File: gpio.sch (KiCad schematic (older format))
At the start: 1 part, among them U1 LFE5U-85F-6BG381C

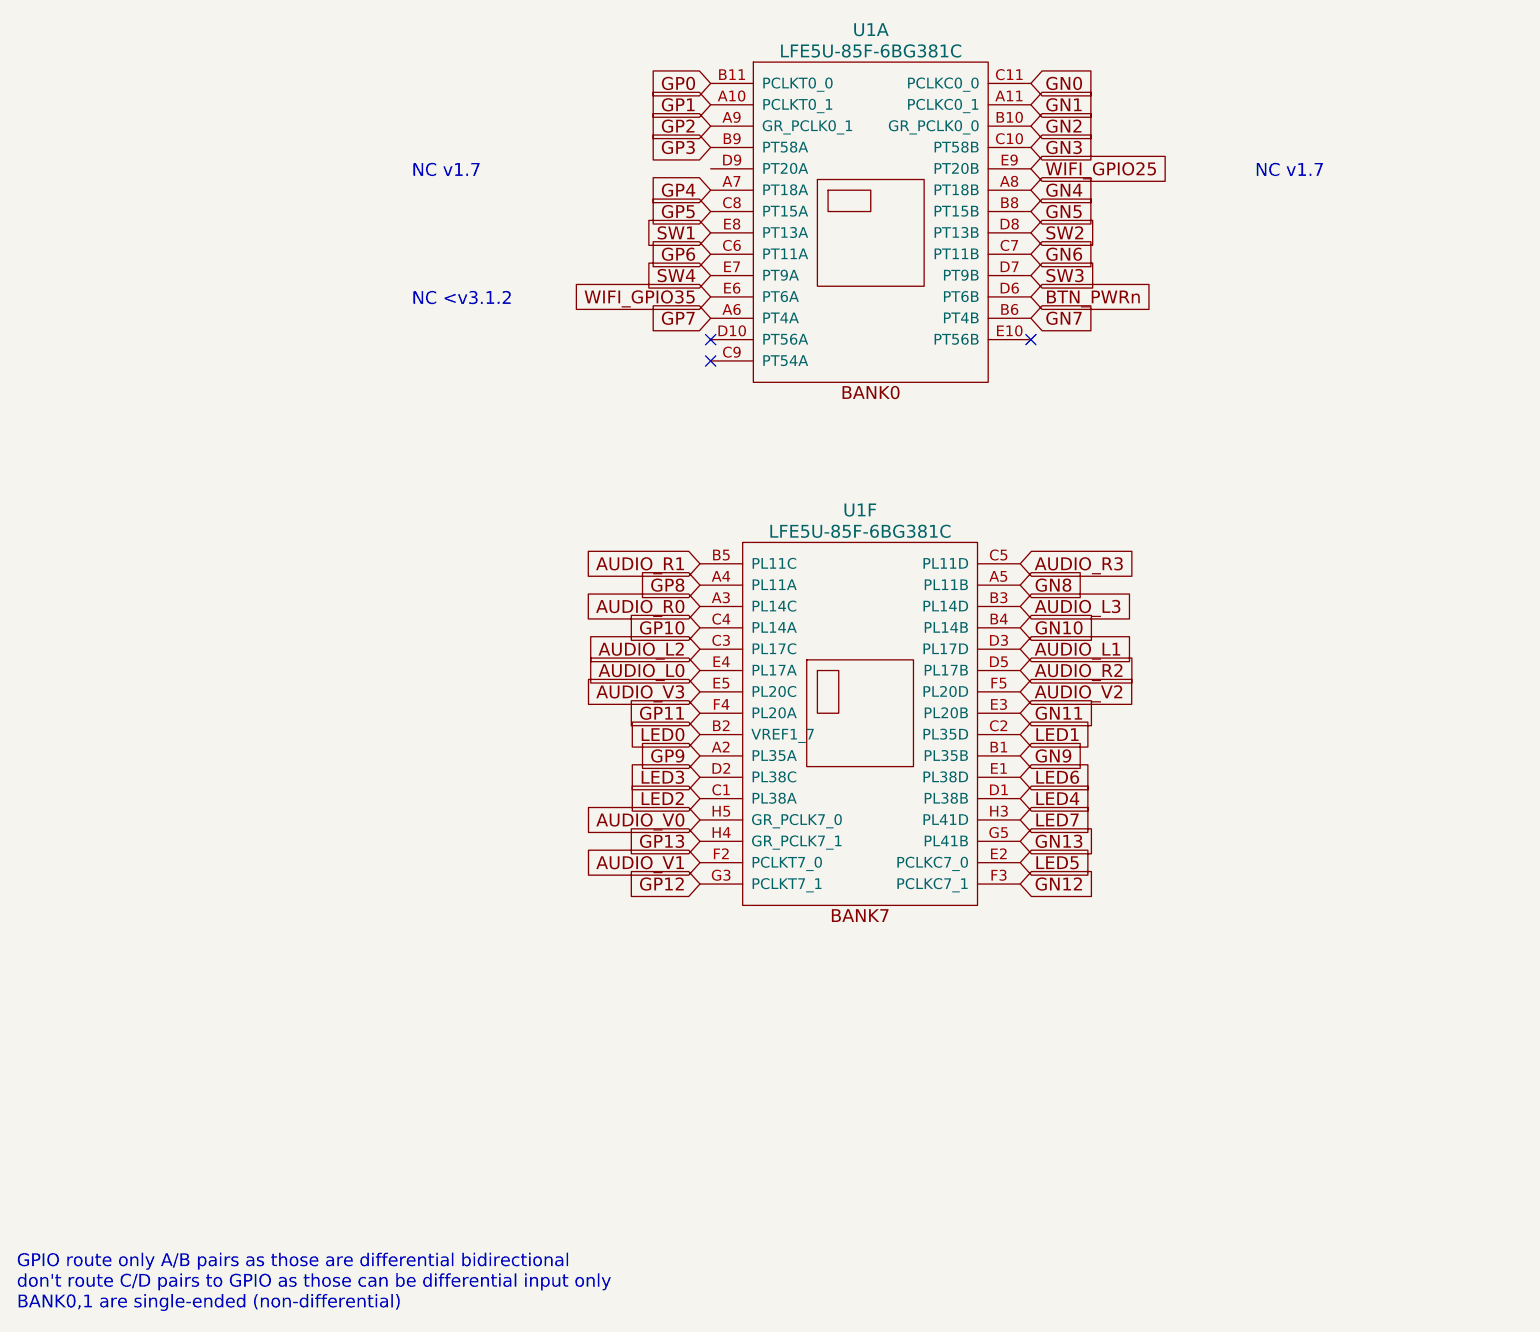
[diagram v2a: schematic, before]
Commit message: Rewiering LCD OUT to bottom left
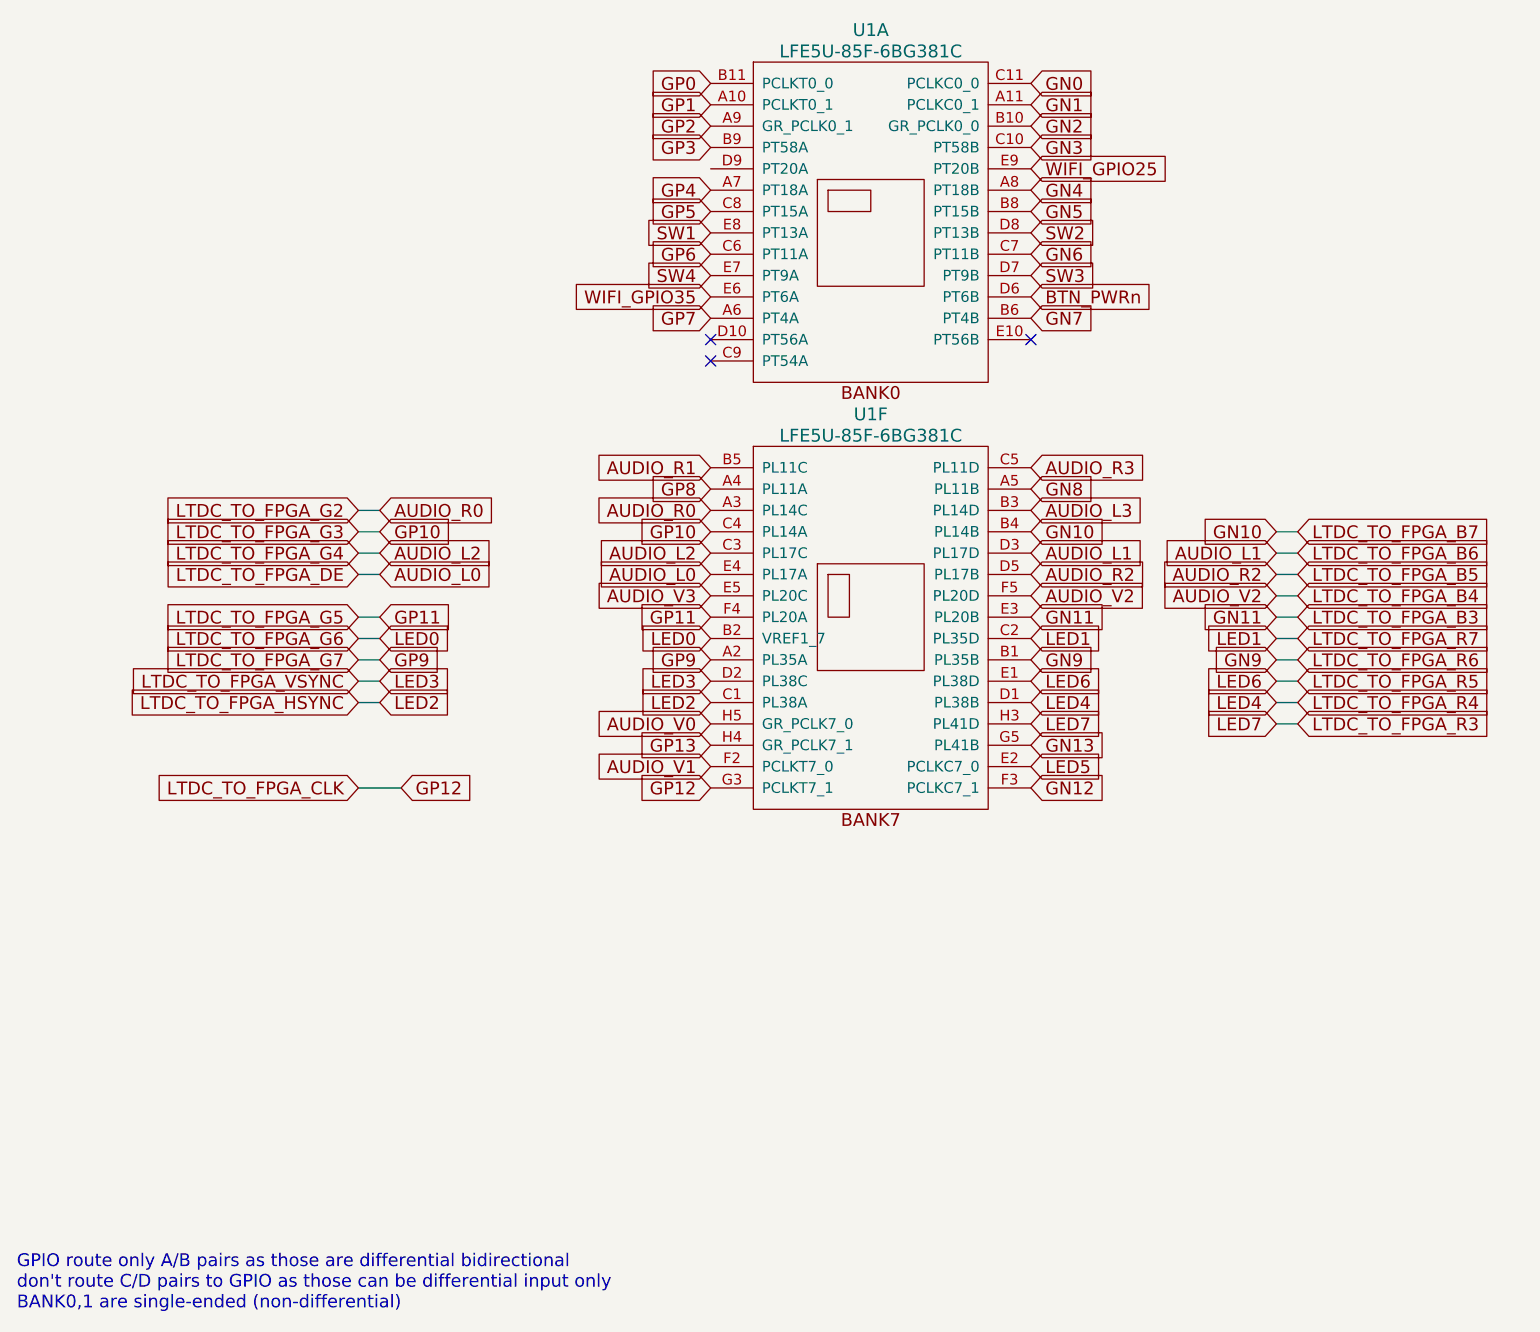
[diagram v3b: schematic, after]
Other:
- note removed: "NC <v3.1.2"
- note removed: "NC v1.7"
- moved on the sheet: U1F
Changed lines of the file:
@@
 Comment4 ""
 $EndDescr
-Text GLabel 5650 5350 2    60   Input ~ 0
+Text GLabel 5700 4900 2    60   Input ~ 0
 GN13
-Text GLabel 4150 5350 0    60   Input ~ 0
+Text GLabel 4200 4900 0    60   Input ~ 0
 GP13
-Text GLabel 4150 5550 0    60   Input ~ 0
+Text GLabel 4200 5100 0    60   Input ~ 0
 GP12
-Text GLabel 5650 5550 2    60   Input ~ 0
+Text GLabel 5700 5100 2    60   Input ~ 0
 GN12
-Text GLabel 5650 4750 2    60   Input ~ 0
+Text GLabel 5700 4300 2    60   Input ~ 0
 GN11
-Text GLabel 4150 4750 0    60   Input ~ 0
+Text GLabel 4200 4300 0    60   Input ~ 0
 GP11
-Text GLabel 5650 4950 2    60   Input ~ 0
+Text GLabel 5700 4500 2    60   Input ~ 0
 GN9
-Text GLabel 4150 4950 0    60   Input ~ 0
+Text GLabel 4200 4500 0    60   Input ~ 0
 GP9
-Text GLabel 5650 4350 2    60   Input ~ 0
+Text GLabel 5700 3900 2    60   Input ~ 0
 GN10
-Text GLabel 4150 4350 0    60   Input ~ 0
+Text GLabel 4200 3900 0    60   Input ~ 0
 GP10
-Text GLabel 5650 4150 2    60   Input ~ 0
+Text GLabel 5700 3700 2    60   Input ~ 0
 GN8
-Text GLabel 4150 4150 0    60   Input ~ 0
+Text GLabel 4200 3700 0    60   Input ~ 0
 GP8
 Text GLabel 5700 2900 2    60   Input ~ 0
@@
 Text GLabel 4200 2100 0    60   Input ~ 0
 GP3
-Text GLabel 4150 4550 0    60   Input ~ 0
+Text GLabel 4200 4100 0    60   Input ~ 0
 AUDIO_L0
-Text GLabel 5650 4450 2    60   Input ~ 0
+Text GLabel 5700 4000 2    60   Input ~ 0
 AUDIO_L1
-Text GLabel 4150 4450 0    60   Input ~ 0
+Text GLabel 4200 4000 0    60   Input ~ 0
 AUDIO_L2
-Text GLabel 5650 4250 2    60   Input ~ 0
+Text GLabel 5700 3800 2    60   Input ~ 0
 AUDIO_L3
-Text GLabel 4150 4250 0    60   Input ~ 0
+Text GLabel 4200 3800 0    60   Input ~ 0
 AUDIO_R0
-Text GLabel 4150 4050 0    60   Input ~ 0
+Text GLabel 4200 3600 0    60   Input ~ 0
 AUDIO_R1
-Text GLabel 5650 4550 2    60   Input ~ 0
+Text GLabel 5700 4100 2    60   Input ~ 0
 AUDIO_R2
-Text GLabel 5650 4050 2    60   Input ~ 0
+Text GLabel 5700 3600 2    60   Input ~ 0
 AUDIO_R3
-Text GLabel 4150 4850 0    60   Input ~ 0
+Text GLabel 4200 4400 0    60   Input ~ 0
 LED0
-Text GLabel 5650 5450 2    60   Input ~ 0
+Text GLabel 5700 5000 2    60   Input ~ 0
 LED5
-Text GLabel 4150 5150 0    60   Input ~ 0
+Text GLabel 4200 4700 0    60   Input ~ 0
 LED2
-Text GLabel 4150 5050 0    60   Input ~ 0
+Text GLabel 4200 4600 0    60   Input ~ 0
 LED3
-Text GLabel 5650 5150 2    60   Input ~ 0
+Text GLabel 5700 4700 2    60   Input ~ 0
 LED4
-Text GLabel 5650 4850 2    60   Input ~ 0
+Text GLabel 5700 4400 2    60   Input ~ 0
 LED1
-Text GLabel 5650 5050 2    60   Input ~ 0
+Text GLabel 5700 4600 2    60   Input ~ 0
 LED6
-Text GLabel 5650 5250 2    60   Input ~ 0
+Text GLabel 5700 4800 2    60   Input ~ 0
 LED7
 Text Notes 950  7550 0    60   ~ 0
@@
 Text GLabel 4200 2700 0    60   Input ~ 0
 SW4
-Text GLabel 4150 4650 0    60   Input ~ 0
+Text GLabel 4200 4200 0    60   Input ~ 0
 AUDIO_V3
-Text GLabel 5650 4650 2    60   Input ~ 0
+Text GLabel 5700 4200 2    60   Input ~ 0
 AUDIO_V2
-Text GLabel 4150 5450 0    60   Input ~ 0
+Text GLabel 4200 5000 0    60   Input ~ 0
 AUDIO_V1
-Text GLabel 4150 5250 0    60   Input ~ 0
+Text GLabel 4200 4800 0    60   Input ~ 0
 AUDIO_V0
 $Comp
 L lfe5bg381:LFE5UM-85F-6BG381C U1
 U 6 1 5A0783C9
-P 4900 4750
+P 4950 4300
 AR Path="/5A0783C9" Ref="U1"  Part="6"
 AR Path="/56AC389C/5A0783C9" Ref="U1"  Part="6"
-F 0 "U1" H 4900 5700 60  0000 C CNN
-F 1 "LFE5U-85F-6BG381C" H 4900 5600 60  0000 C CNN
-F 2 "lfe5bg381:BGA-381_pitch0.8mm_dia0.4mm" H 3850 5700 60  0001 C CNN
-F 3 "http://www.latticesemi.com/~/media/LatticeSemi/Documents/DataSheets/ECP5/FPGA-DS-02012.pdf" H 3850 5700 60  0001 C CNN
-F 4 "LFE5U-85F-6BG381C" H 4900 4750 60  0001 C CNN "MPN"
-F 5 "842-LFE5U85F6BG381C" H 4900 4750 60  0001 C CNN "Mouser"
-	6    4900 4750
+F 0 "U1" H 4950 5250 60  0000 C CNN
+F 1 "LFE5U-85F-6BG381C" H 4950 5150 60  0000 C CNN
+F 2 "lfe5bg381:BGA-381_pitch0.8mm_dia0.4mm" H 3900 5250 60  0001 C CNN
+F 3 "http://www.latticesemi.com/~/media/LatticeSemi/Documents/DataSheets/ECP5/FPGA-DS-02012.pdf" H 3900 5250 60  0001 C CNN
+F 4 "LFE5U-85F-6BG381C" H 4950 4300 60  0001 C CNN "MPN"
+F 5 "842-LFE5U85F6BG381C" H 4950 4300 60  0001 C CNN "Mouser"
+	6    4950 4300
 	1    0    0    -1
 $EndComp
@@
 	1    0    0    -1
 $EndComp
-Text Notes 2800 2250 0    60   ~ 0
-NC v1.7
-Text Notes 6750 2250 0    60   ~ 0
-NC v1.7
 NoConn ~ 4200 3000
 NoConn ~ 4200 3100
@@
 Text GLabel 5700 2200 2    60   Input ~ 0
 WIFI_GPIO25
+Text GLabel 6950 4800 2    60   Input ~ 0
+LTDC_TO_FPGA_R3
+Text GLabel 6950 4700 2    60   Input ~ 0
+LTDC_TO_FPGA_R4
+Text GLabel 6950 4600 2    60   Input ~ 0
+LTDC_TO_FPGA_R5
+Text GLabel 6950 4500 2    60   Input ~ 0
+LTDC_TO_FPGA_R6
+Text GLabel 6950 4400 2    60   Input ~ 0
+LTDC_TO_FPGA_R7
+Text GLabel 2550 3900 0    60   Input ~ 0
+LTDC_TO_FPGA_G3
+Text GLabel 2550 4000 0    60   Input ~ 0
+LTDC_TO_FPGA_G4
+Text GLabel 2550 4300 0    60   Input ~ 0
+LTDC_TO_FPGA_G5
+Text GLabel 2550 4400 0    60   Input ~ 0
+LTDC_TO_FPGA_G6
+Text GLabel 2550 4500 0    60   Input ~ 0
+LTDC_TO_FPGA_G7
+Text GLabel 6950 3900 2    60   Input ~ 0
+LTDC_TO_FPGA_B7
+Text GLabel 6950 4000 2    60   Input ~ 0
+LTDC_TO_FPGA_B6
+Text GLabel 6950 4100 2    60   Input ~ 0
+LTDC_TO_FPGA_B5
+Text GLabel 6950 4200 2    60   Input ~ 0
+LTDC_TO_FPGA_B4
+Text GLabel 6950 4300 2    60   Input ~ 0
+LTDC_TO_FPGA_B3
+Text GLabel 2550 3800 0    60   Input ~ 0
+LTDC_TO_FPGA_G2
+Text GLabel 2550 5100 0    60   Input ~ 0
+LTDC_TO_FPGA_CLK
+Text GLabel 2550 4100 0    60   Input ~ 0
+LTDC_TO_FPGA_DE
+Text GLabel 2550 4700 0    60   Input ~ 0
+LTDC_TO_FPGA_HSYNC
+Text GLabel 2550 4600 0    60   Input ~ 0
+LTDC_TO_FPGA_VSYNC
+Text GLabel 2750 5100 2    60   Input ~ 0
+GP12
+Wire Wire Line
+	2750 5100 2550 5100
 Text GLabel 4200 2800 0    60   Input ~ 0
 WIFI_GPIO35
-Text Notes 2800 2850 0    60   ~ 0
-NC <v3.1.2
+Text GLabel 2650 3800 2    60   Input ~ 0
+AUDIO_R0
+Text GLabel 2650 3900 2    60   Input ~ 0
+GP10
+Text GLabel 2650 4000 2    60   Input ~ 0
+AUDIO_L2
+Text GLabel 2650 4100 2    60   Input ~ 0
+AUDIO_L0
+Text GLabel 2650 4300 2    60   Input ~ 0
+GP11
+Text GLabel 2650 4400 2    60   Input ~ 0
+LED0
+Text GLabel 2650 4500 2    60   Input ~ 0
+GP9
+Text GLabel 2650 4600 2    60   Input ~ 0
+LED3
+Text GLabel 2650 4700 2    60   Input ~ 0
+LED2
+Wire Wire Line
+	2550 3800 2650 3800
+Wire Wire Line
+	2650 3900 2550 3900
+Wire Wire Line
+	2550 4000 2650 4000
+Wire Wire Line
+	2650 4100 2550 4100
+Wire Wire Line
+	2550 4300 2650 4300
+Wire Wire Line
+	2650 4400 2550 4400
+Wire Wire Line
+	2550 4500 2650 4500
+Wire Wire Line
+	2650 4600 2550 4600
+Wire Wire Line
+	2550 4700 2650 4700
+Text GLabel 6850 3900 0    60   Input ~ 0
+GN10
+Text GLabel 6850 4000 0    60   Input ~ 0
+AUDIO_L1
+Text GLabel 6850 4100 0    60   Input ~ 0
+AUDIO_R2
+Text GLabel 6850 4200 0    60   Input ~ 0
+AUDIO_V2
+Text GLabel 6850 4300 0    60   Input ~ 0
+GN11
+Text GLabel 6850 4400 0    60   Input ~ 0
+LED1
+Text GLabel 6850 4500 0    60   Input ~ 0
+GN9
+Text GLabel 6850 4600 0    60   Input ~ 0
+LED6
+Text GLabel 6850 4700 0    60   Input ~ 0
+LED4
+Text GLabel 6850 4800 0    60   Input ~ 0
+LED7
+Wire Wire Line
+	6850 3900 6950 3900
+Wire Wire Line
+	6850 4000 6950 4000
+Wire Wire Line
+	6850 4100 6950 4100
+Wire Wire Line
+	6850 4200 6950 4200
+Wire Wire Line
+	6850 4300 6950 4300
+Wire Wire Line
+	6850 4400 6950 4400
+Wire Wire Line
+	6850 4500 6950 4500
+Wire Wire Line
+	6850 4600 6950 4600
+Wire Wire Line
+	6850 4700 6950 4700
+Wire Wire Line
+	6850 4800 6950 4800
 $EndSCHEMATC

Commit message: better RGB-OUT
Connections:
- net GP10 renamed LTDC_TO_FPGA_G3
- net LED0 renamed LTDC_TO_FPGA_G6
- net WIFI_GPIO25 renamed LTDC_FROM_FPGA_R5
- net WIFI_GPIO35 renamed LTDC_FROM_FPGA_R3
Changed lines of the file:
@@
 Text GLabel 5700 3900 2    60   Input ~ 0
 GN10
-Text GLabel 4200 3900 0    60   Input ~ 0
-GP10
 Text GLabel 5700 3700 2    60   Input ~ 0
 GN8
@@
 Text GLabel 5700 3600 2    60   Input ~ 0
 AUDIO_R3
-Text GLabel 4200 4400 0    60   Input ~ 0
-LED0
 Text GLabel 5700 5000 2    60   Input ~ 0
 LED5
@@
 NoConn ~ 4200 3100
 NoConn ~ 5700 3000
-Text GLabel 5700 2200 2    60   Input ~ 0
-WIFI_GPIO25
 Text GLabel 6950 4800 2    60   Input ~ 0
 LTDC_TO_FPGA_R3
@@
 Text GLabel 6950 4400 2    60   Input ~ 0
 LTDC_TO_FPGA_R7
-Text GLabel 2550 3900 0    60   Input ~ 0
+Text GLabel 4200 3900 0    60   Input ~ 0
 LTDC_TO_FPGA_G3
 Text GLabel 2550 4000 0    60   Input ~ 0
@@
 Text GLabel 2550 4300 0    60   Input ~ 0
 LTDC_TO_FPGA_G5
-Text GLabel 2550 4400 0    60   Input ~ 0
+Text GLabel 4200 4400 0    60   Input ~ 0
 LTDC_TO_FPGA_G6
 Text GLabel 2550 4500 0    60   Input ~ 0
@@
 Wire Wire Line
 	2750 5100 2550 5100
-Text GLabel 4200 2800 0    60   Input ~ 0
-WIFI_GPIO35
 Text GLabel 2650 3800 2    60   Input ~ 0
 AUDIO_R0
-Text GLabel 2650 3900 2    60   Input ~ 0
-GP10
 Text GLabel 2650 4000 2    60   Input ~ 0
 AUDIO_L2
@@
 Text GLabel 2650 4300 2    60   Input ~ 0
 GP11
-Text GLabel 2650 4400 2    60   Input ~ 0
-LED0
 Text GLabel 2650 4500 2    60   Input ~ 0
 GP9
@@
 	2550 3800 2650 3800
 Wire Wire Line
-	2650 3900 2550 3900
-Wire Wire Line
 	2550 4000 2650 4000
 Wire Wire Line
@@
 Wire Wire Line
 	2550 4300 2650 4300
-Wire Wire Line
-	2650 4400 2550 4400
 Wire Wire Line
 	2550 4500 2650 4500
@@
 Wire Wire Line
 	6850 4800 6950 4800
+Text GLabel 4100 2800 0    60   Input ~ 0
+LTDC_FROM_FPGA_R3
+Wire Wire Line
+	4100 2800 4200 2800
+Text GLabel 5700 2200 2    60   Input ~ 0
+LTDC_FROM_FPGA_R5
 $EndSCHEMATC
